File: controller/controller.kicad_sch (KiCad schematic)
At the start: 20 parts, among them J2 Conn_01x03_Socket, J3 WAGO 236-402, J4 WAGO 236-402, J5 WAGO 236-404, Q1 2N2222

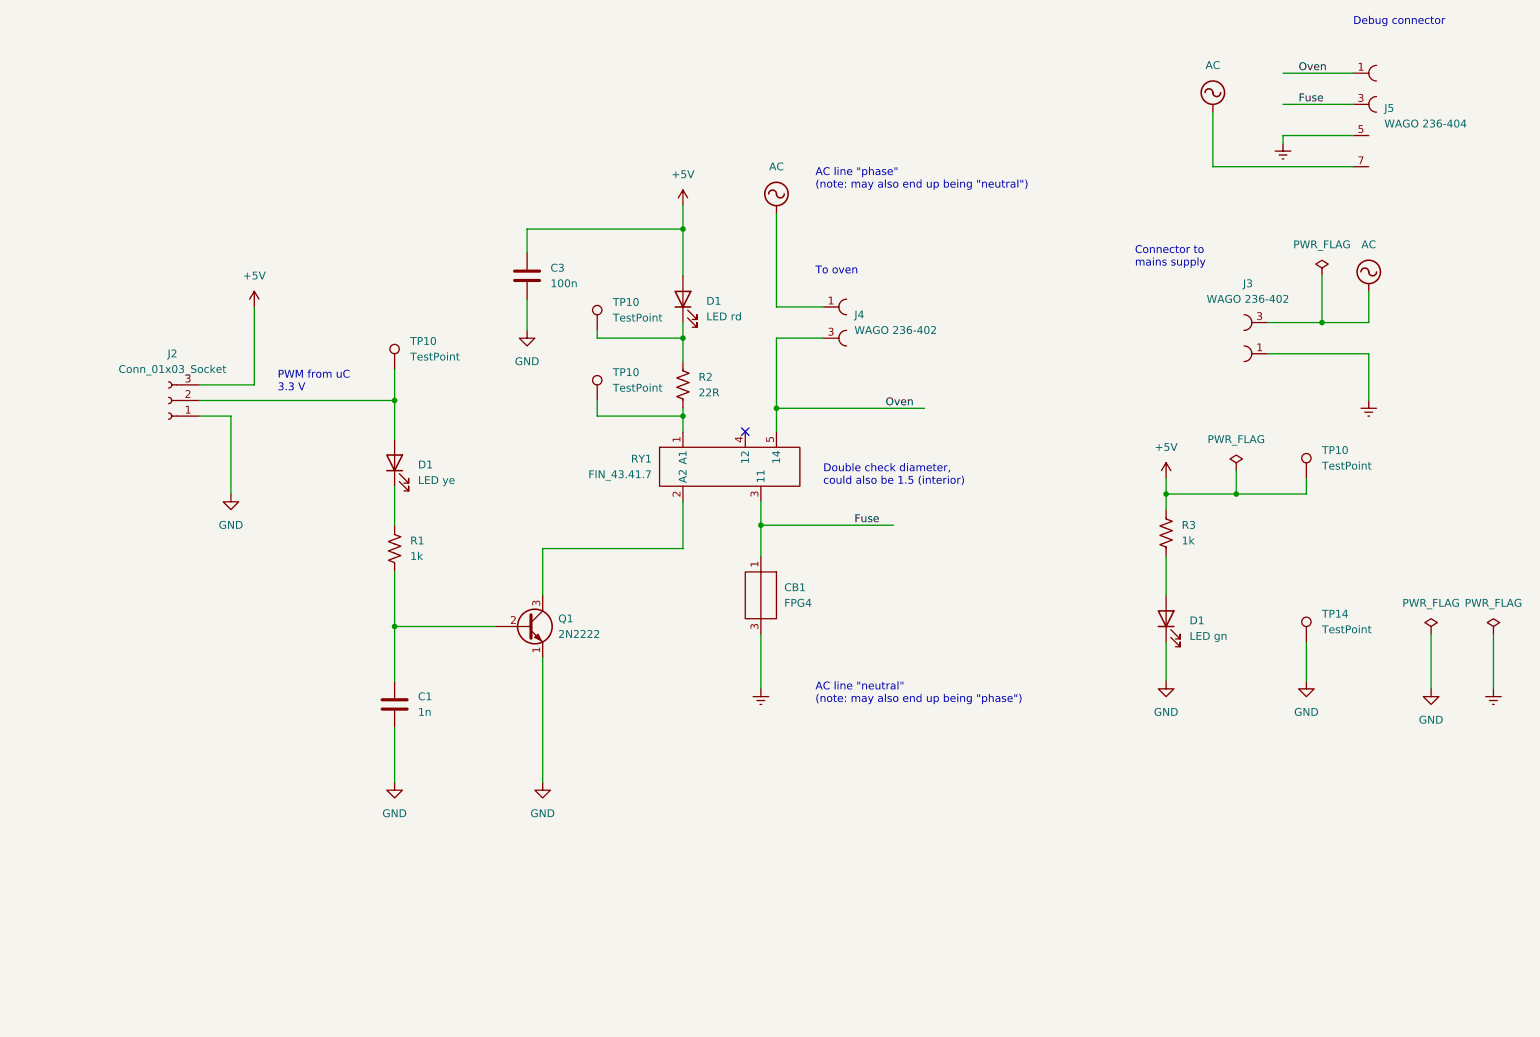
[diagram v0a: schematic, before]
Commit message: Incorporated changes to the reflow controller schematic (v1.0.0 to v1.0.1)
Also incorporated some changes to the board, but did not place
and route the two additional resistors.
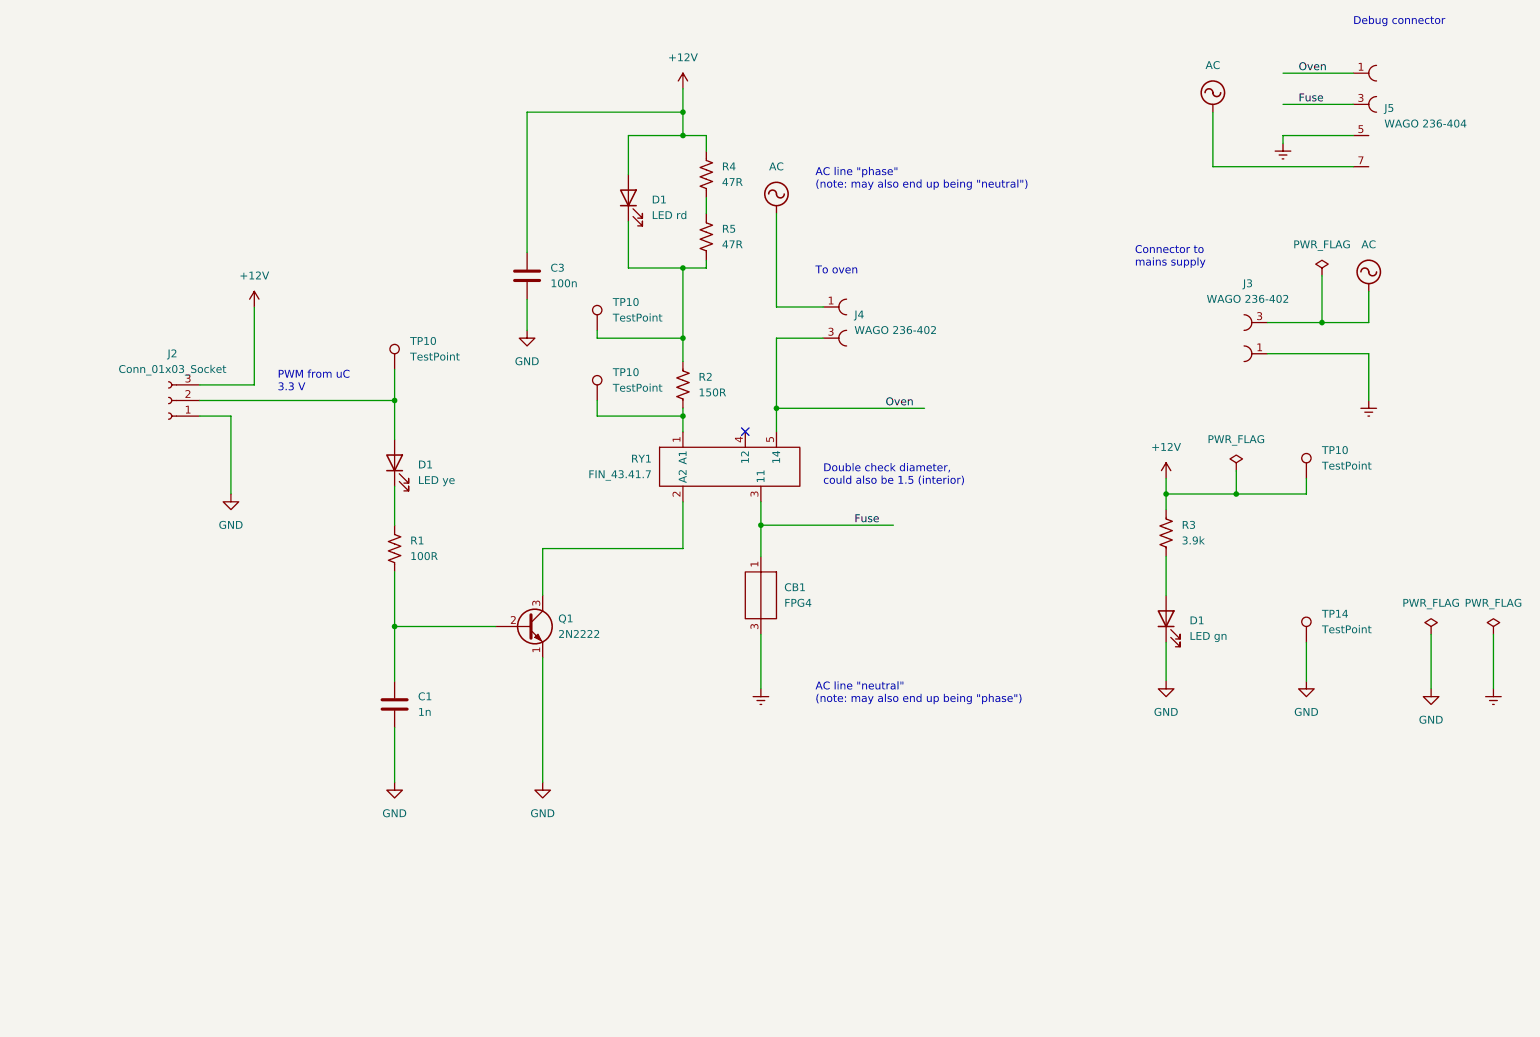
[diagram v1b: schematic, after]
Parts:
- added R4, R5: 47R, Resistor_THT:R_Axial_DIN0207_L6.3mm_D2.5mm_P10.16mm_Horizontal, symbol Device:R_US
- R1: value 1k -> 100R
- R2: value 22R -> 150R
- R3: value 1k -> 3.9k
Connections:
- net at D1.1 (K), R2.1, TP10.1: now also R5.2
- net +5V renamed +12V
- net +12V: now also R4.1
- new net: R4.2, R5.1
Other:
- moved on the sheet: D1

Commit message: Added schematic for thermocouple amplifier
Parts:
- renumbered C3 to C2, J2 to J1, J4 to J2, J5 to J4, R4 to R3, R5 to R4, R3 to R5
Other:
- added sheet Thermo amplifier (thermoamp.kicad_sch)
